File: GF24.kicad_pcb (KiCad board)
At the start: 2 copper layers, 110 x 40 mm, 66 parts, among them J1 3220-10-0300-00, Q1 3904, Q2 DMN3731U-7, Q3 DMN3731U-7, Q4 DMP2004K-7, Q5 DMP2004K-7, Q6 DMP2004K-7, SW1 NRST, SW2 BOOT, SW3 ACTION, SW4 ON/OFF, SW5 MODE, U1 STM32F031C4T6, U2 SAM-M10Q, U3 TPS745, U4 LTC1733, U5 M24256, U6 2137160001, Y1 CS06465-32M

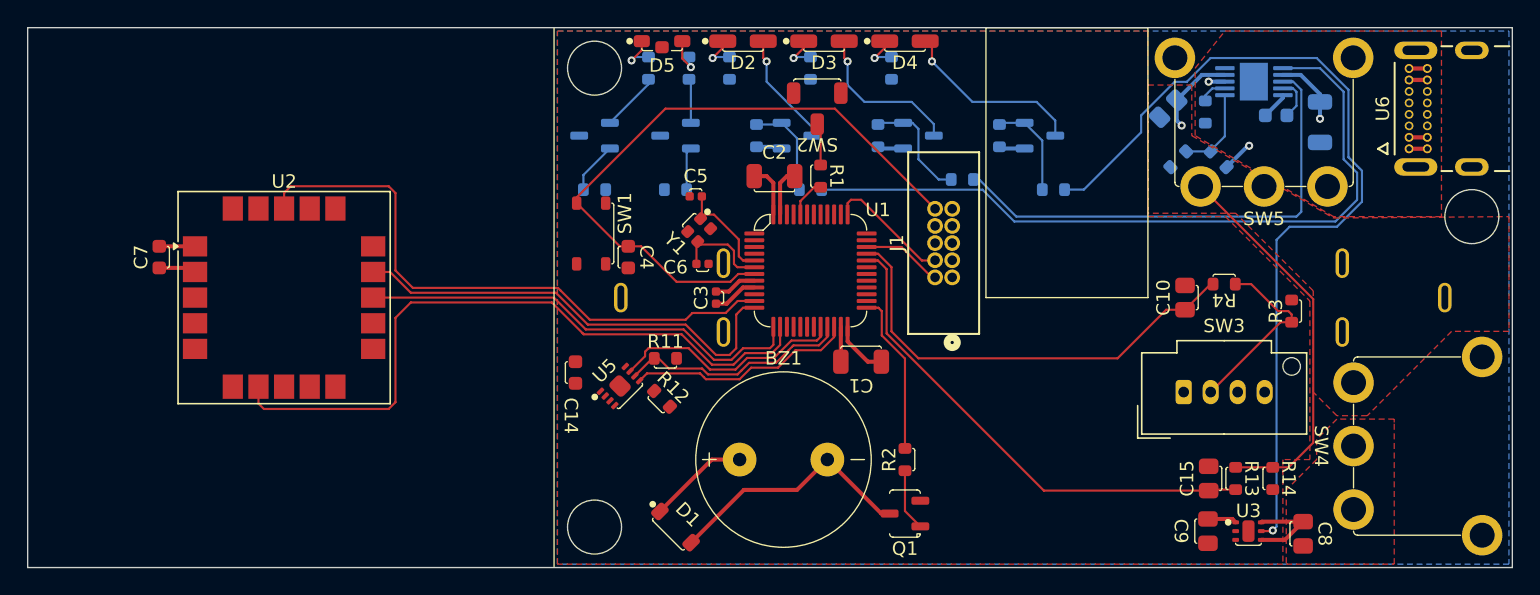
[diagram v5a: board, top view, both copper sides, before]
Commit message: fixed some small ERC/DRC issues
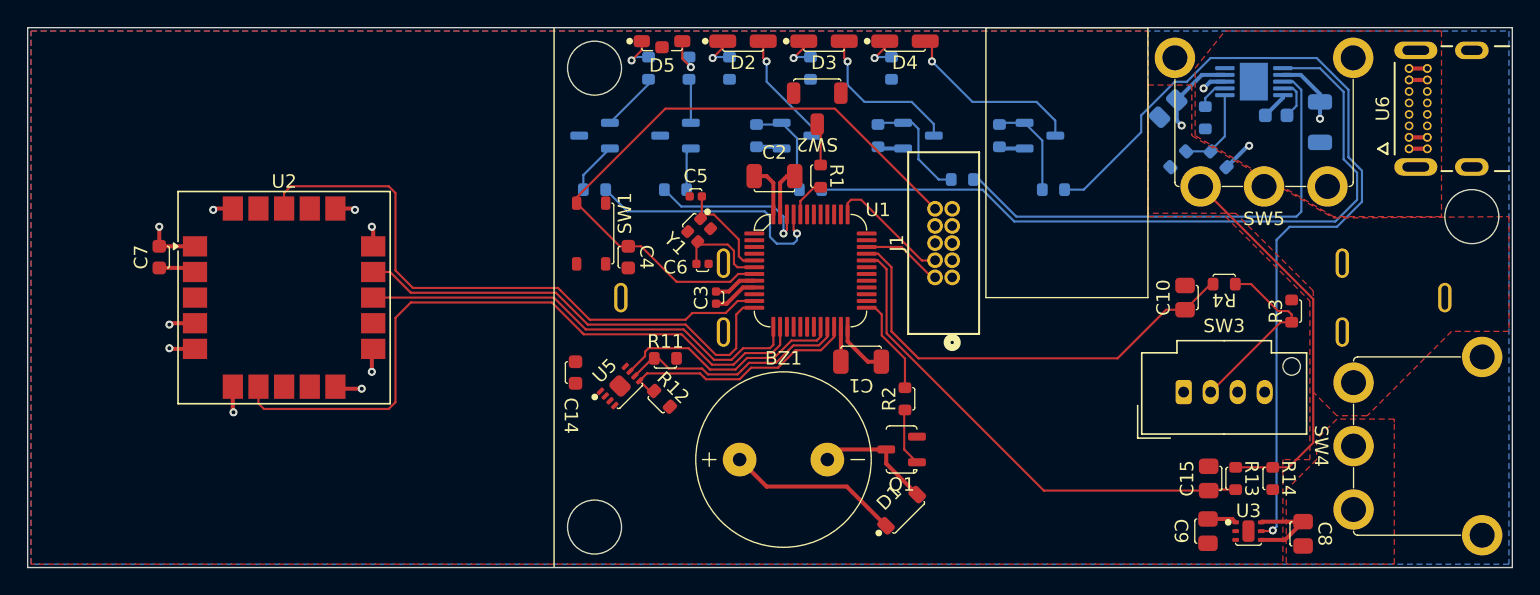
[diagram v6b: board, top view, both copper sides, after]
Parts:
- moved D1 16.8 mm to (140.8, 110.8), turned to 45 degrees
- moved Q1 4.76 mm to (140.8, 106.2)
- moved R2 4.50 mm to (141.0, 102.5)
- moved R5 0.42 mm to (163.2, 81.7)
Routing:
- net STATR: track 0.00 -> 18.8 mm, vias 0 -> 1
- net GND: track 14.1 -> 29.5 mm, vias 0 -> 9
- net STATG: track 0.00 -> 12.4 mm, vias 0 -> 1
- net /BUZZ-: track 18.9 -> 8.97 mm
- net 3V3: track 25.8 -> 31.2 mm
- net BUZZER: track 12.1 -> 7.46 mm
- net SDA: track 16.9 -> 18.3 mm
- net VBUS: track 12.5 -> 13.1 mm

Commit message: updated power planes
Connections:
- U5 pad 9: (no net) -> GND
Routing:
- net GND: track 29.5 -> 60.3 mm, vias 9 -> 24
- net 3V3: track 31.2 -> 36.0 mm, vias 0 -> 1
- net MODE: track 37.2 -> 41.0 mm
- net /MODE-H: track 28.9 -> 32.0 mm
- net VBUS: track 13.1 -> 11.8 mm
- net (no net): vias 0 -> 1

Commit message: possibly done with routing
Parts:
- removed C7: 0.1uF, MB-Generic:C0603_medium
- moved SW2 1.27 mm to (134.8, 82.2)
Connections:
- U5 pad 9: GND -> (no net)
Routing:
- net GND: track 60.3 -> 71.3 mm, vias 24 -> 34
- net NRST: track 48.6 -> 45.5 mm
- net VBUS: track 11.8 -> 13.4 mm, vias 3 -> 5
- net /BOOT0_RES: track 3.13 -> 1.77 mm
- net 3V3: track 36.0 -> 35.7 mm, vias 1 -> 3
- net (no net): vias 1 -> 0
